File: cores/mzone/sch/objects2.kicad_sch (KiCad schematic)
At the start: 16 parts

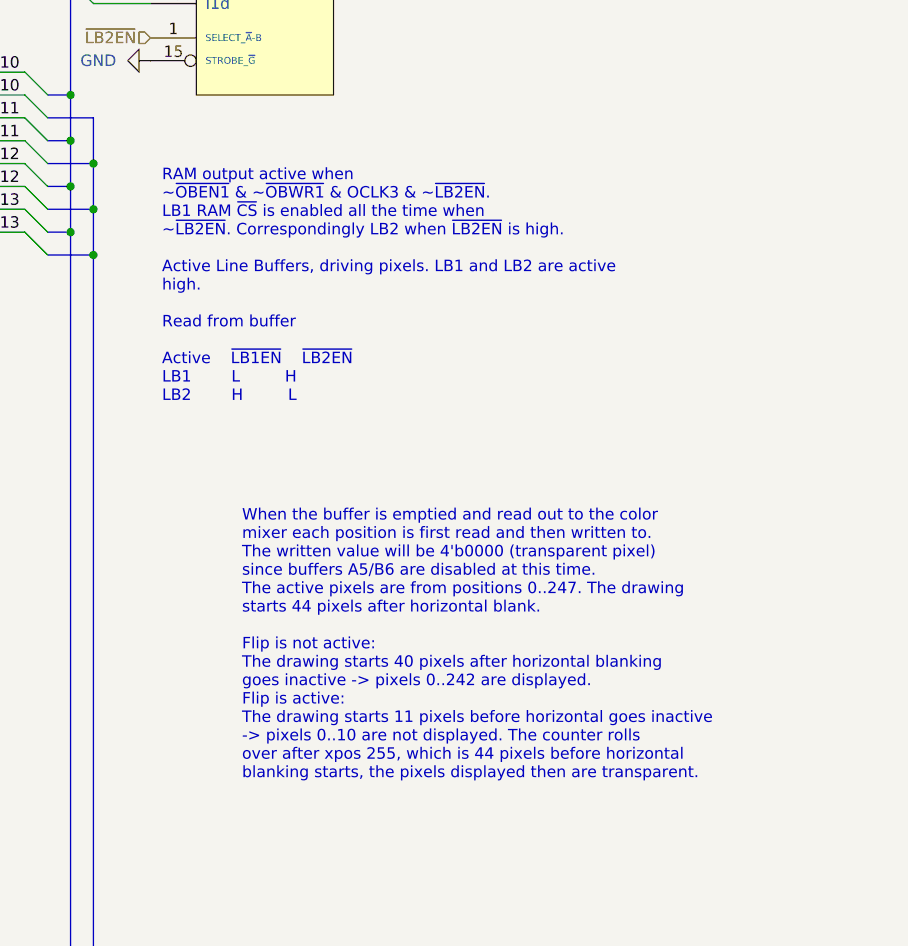
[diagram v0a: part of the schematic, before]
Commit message: mzone core
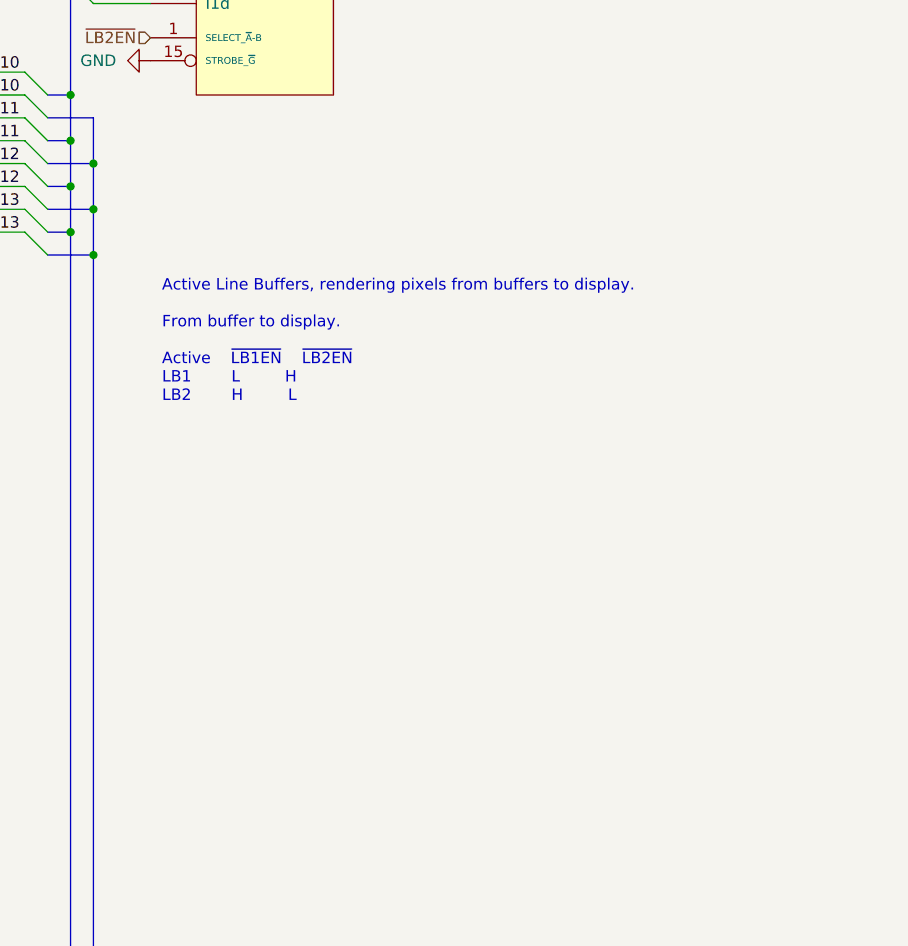
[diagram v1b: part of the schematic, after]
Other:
- note added: "Active Line Buffers, rendering pixels from buffers to display. From buffer to display. Active ~{LB1EN} ~{LB2EN} LB1 L H LB2 H L"
- note removed: "RAM output active when ~~{OBEN1} & ~~{OBWR1} & OCLK3 & ~~{LB2EN}. LB1 RAM ~{CS} is enabled all the time when ~~{LB2EN}. Correspondingly LB2 when ~{LB2EN} is high. Active Line Buffers, driving pixels. LB1 and LB2 are active high. Read from buffer Active ~{LB1EN} ~{LB2EN} LB1 L H LB2 H L"
- note removed: "When the buffer is emptied and read out to the color mixer each position is first read and then written to. The written value will be 4'b0000 (transparent pixel) since buffers A5/B6 are disabled at this time. The active pixels are from positions 0..247. The drawing starts 44 pixels after horizontal blank. Flip is not active: The drawing starts 40 pixels after horizontal blanking goes inactive -> 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"
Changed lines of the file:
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@@
 		)
 	)
-	(text "RAM output active when\n~~{OBEN1} & ~~{OBWR1} & OCLK3 & ~~{LB2EN}.\nLB1 RAM ~{CS} is enabled all the time when\n~~{LB2EN}. Correspondingly LB2 when ~{LB2EN} is high.\n\nActive Line Buffers, driving pixels. LB1 and LB2 are active\nhigh.\n\nRead from buffer\n\nActive	~{LB1EN}	~{LB2EN}\nLB1		L		 H\nLB2		H		 L\n"
+	(text "Active Line Buffers, rendering pixels from buffers to display.\n\nFrom buffer to display.\n\nActive	~{LB1EN}	~{LB2EN}\nLB1		L		 H\nLB2		H		 L\n"
 		(exclude_from_sim no)
 		(at 312.42 166.37 0)
@@
 		(effects
 			(font
-				(size 1.27 1.27)
-			)
-			(justify left bottom)
-		)
-	)
-	(text "When the buffer is emptied and read out to the color\nmixer each position is first read and then written to.\nThe written value will be 4'b0000 (transparent pixel)\nsince buffers A5/B6 are disabled at this time.\nThe active pixels are from positions 0..247. The drawing\nstarts 44 pixels after horizontal blank.\n\nFlip is not active:\nThe drawing starts 40 pixels after horizontal blanking\ngoes inactive -> pixels 0..242 are displayed.\nFlip is active:\nThe drawing starts 11 pixels before horizontal goes inactive\n-> pixels 0..10 are not displayed. The counter rolls\nover after xpos 255, which is 44 pixels before horizontal\nblanking starts, the pixels displayed then are transparent."
-		(exclude_from_sim no)
-		(at 321.31 208.28 0)
-		(effects
-			(font

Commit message: mzone core
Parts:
- added unit 2 of A6
- added unit 2 of B5
- added unit 2 of B7
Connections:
- net GND: now also A6.8 (GND), B5.10 (GND), B7.8 (GND)
- net VCC: now also A6.16 (VCC), B5.20 (VCC), B7.16 (VCC); no longer B5.20 (VCC)
- removed net VSS: B5.10 (VSS)

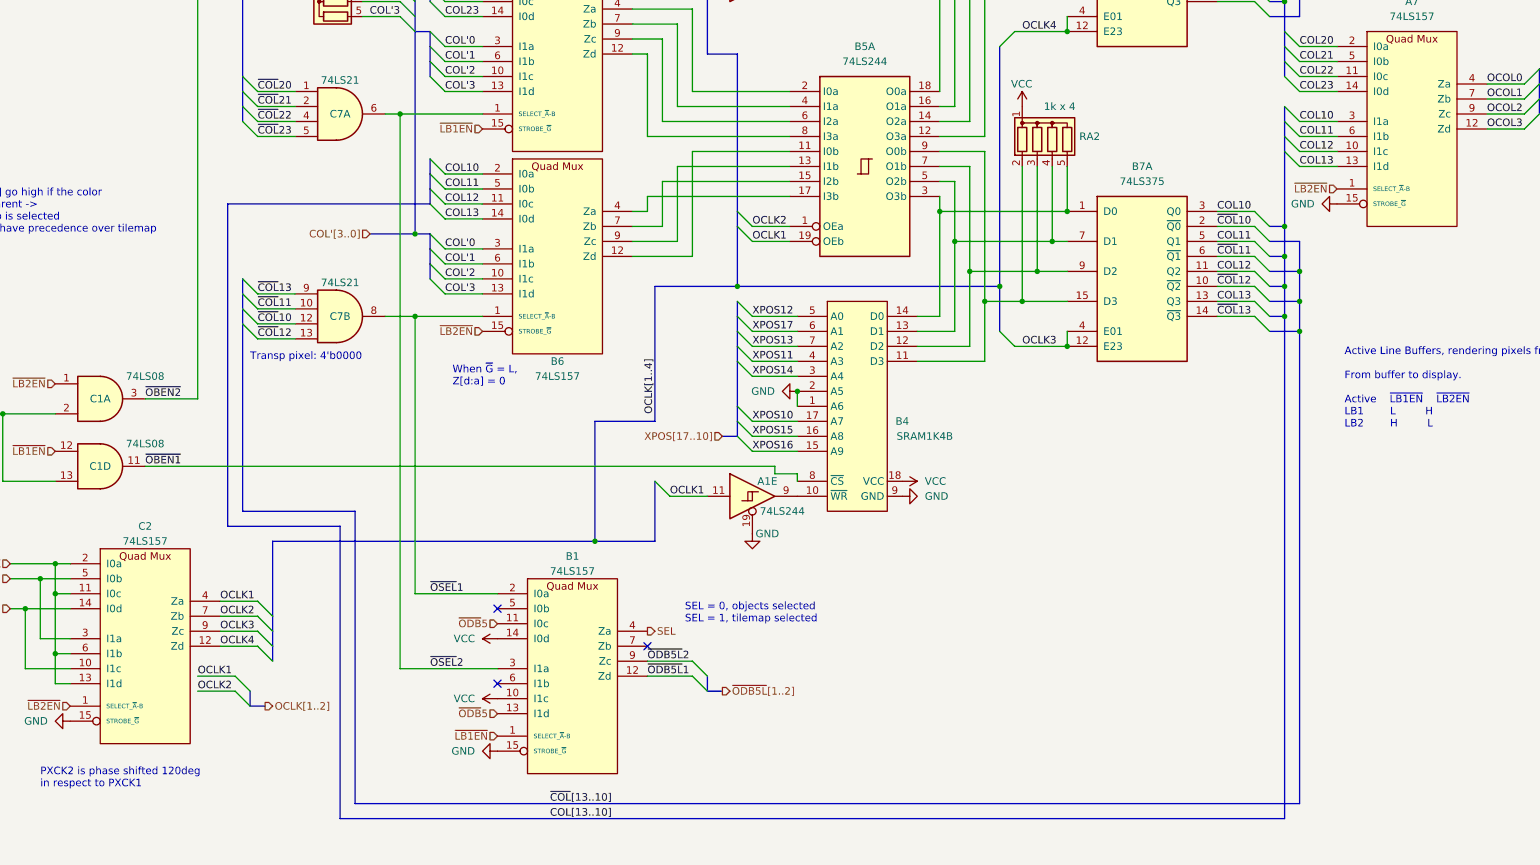
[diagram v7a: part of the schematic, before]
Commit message: mzone core
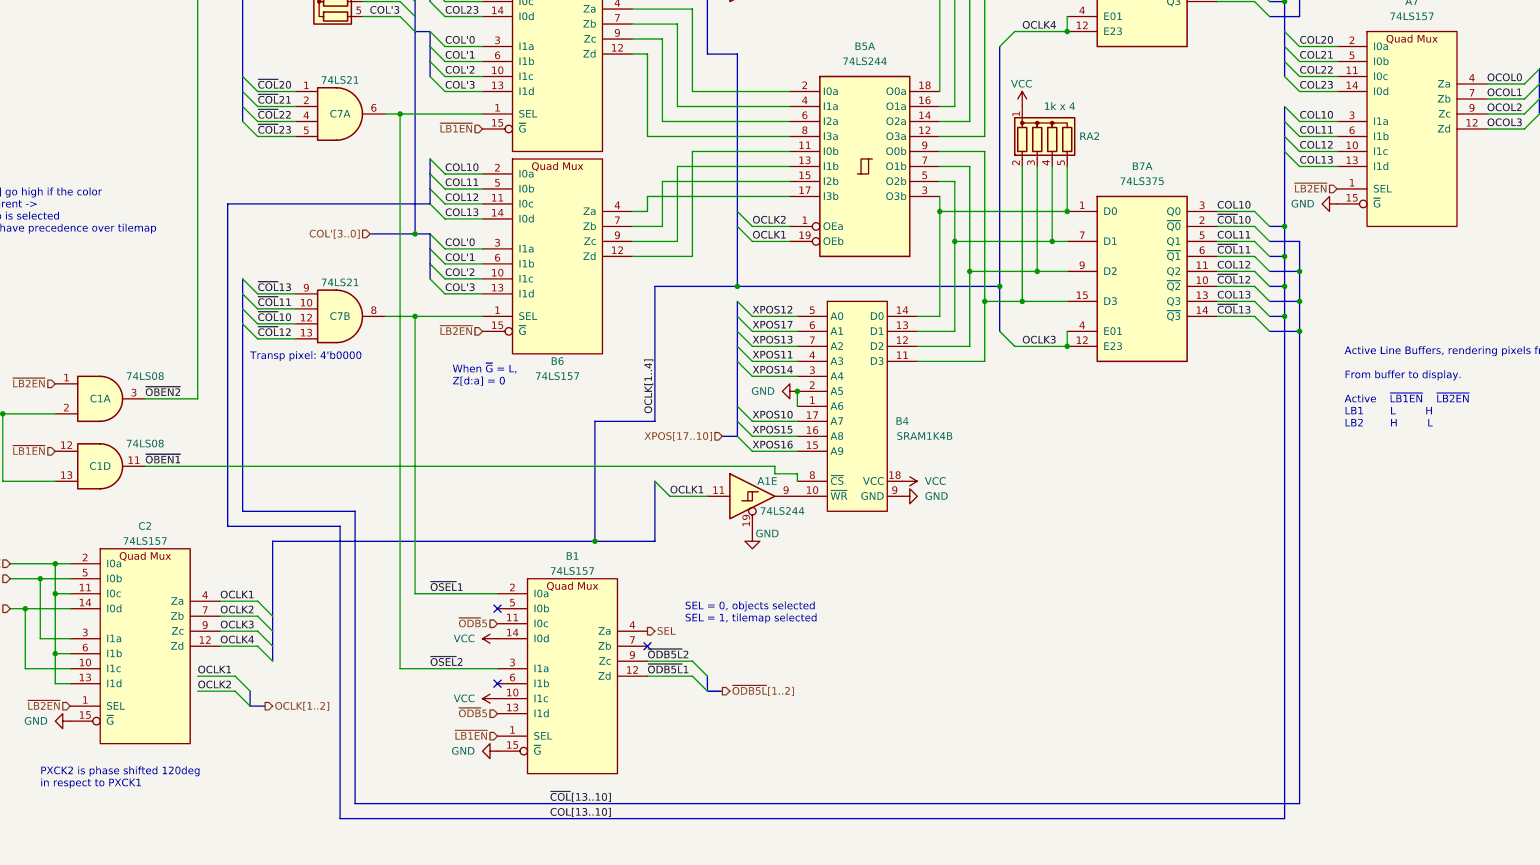
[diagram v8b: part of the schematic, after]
